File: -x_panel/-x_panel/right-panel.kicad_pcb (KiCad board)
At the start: 2 copper layers, 85 x 270 mm, 12 parts

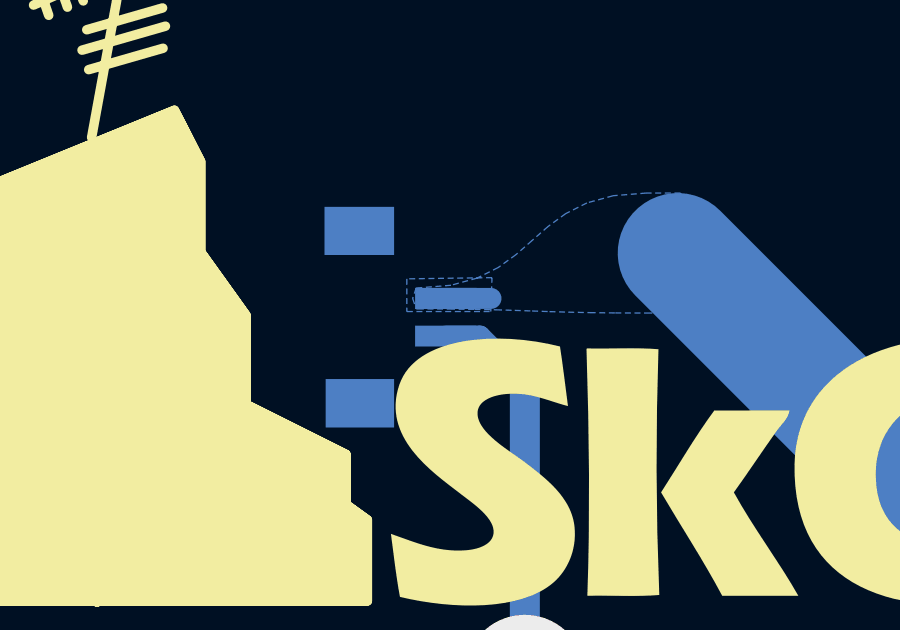
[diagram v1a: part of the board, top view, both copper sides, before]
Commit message: Removed GND and PWR plane, replaced with traces, switches are now in series rather than in parallel
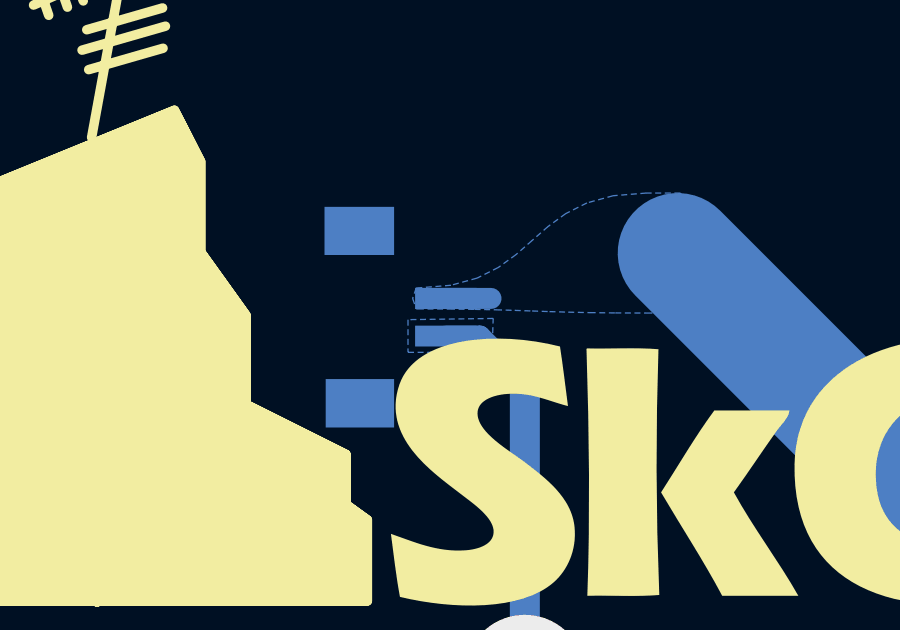
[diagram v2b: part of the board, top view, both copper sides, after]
